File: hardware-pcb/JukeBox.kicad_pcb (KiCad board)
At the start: 2 copper layers, 100 x 100 mm, 97 parts, among them J1 USB4105-GF-A, Q1 Q_NPN_ECB, SW1 SW_SPST, SW10 SW_SPST, SW11 SW_SPST, SW12 SW_SPST, SW2 SW_SPST, SW3 SW_SPST, SW4 SW_SPST, SW5 SW_SPST, SW6 SW_SPST, SW7 SW_SPST, SW8 SW_SPST, SW9 SW_SPST, U1 NCP1117-3.3_SOT223, U2 W25Q128JVS, U3 RP2040, U4 st7789v, Y1 ECS-120-20-33-AEL-TR

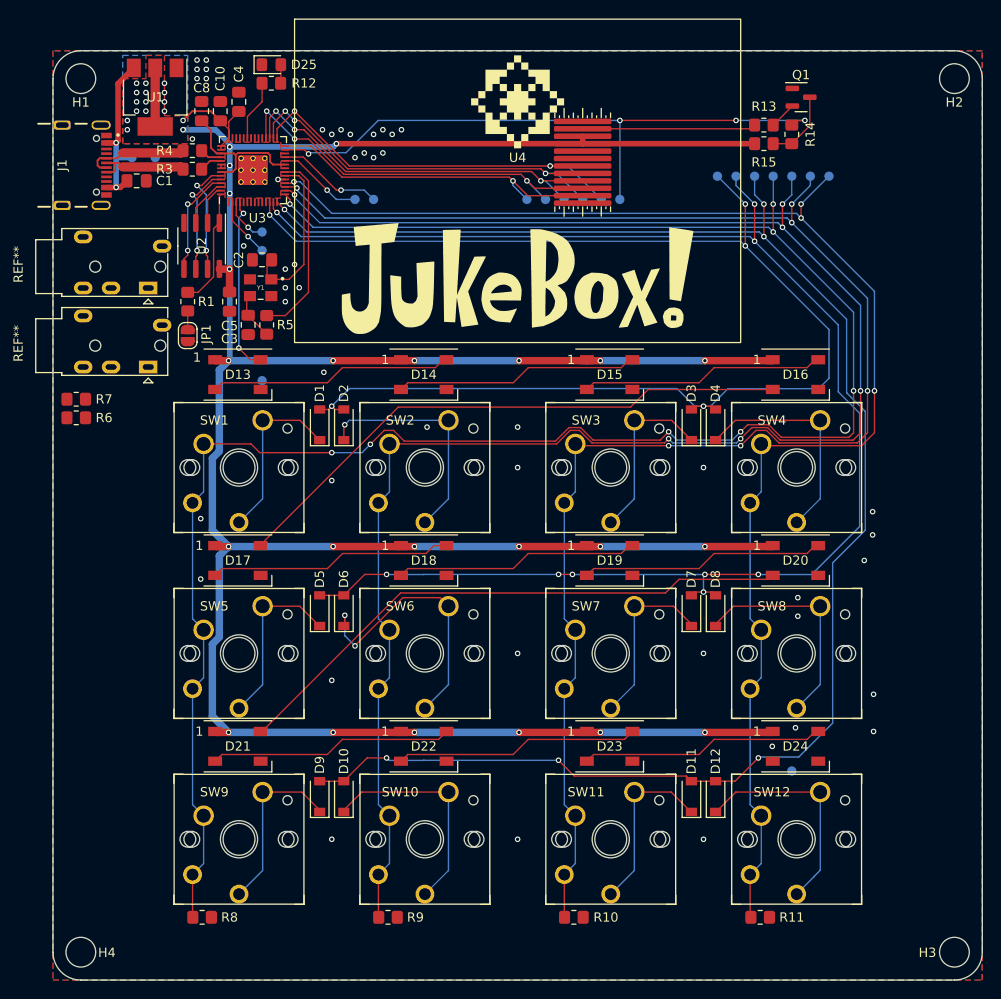
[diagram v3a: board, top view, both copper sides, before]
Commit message: change mounting to via pads
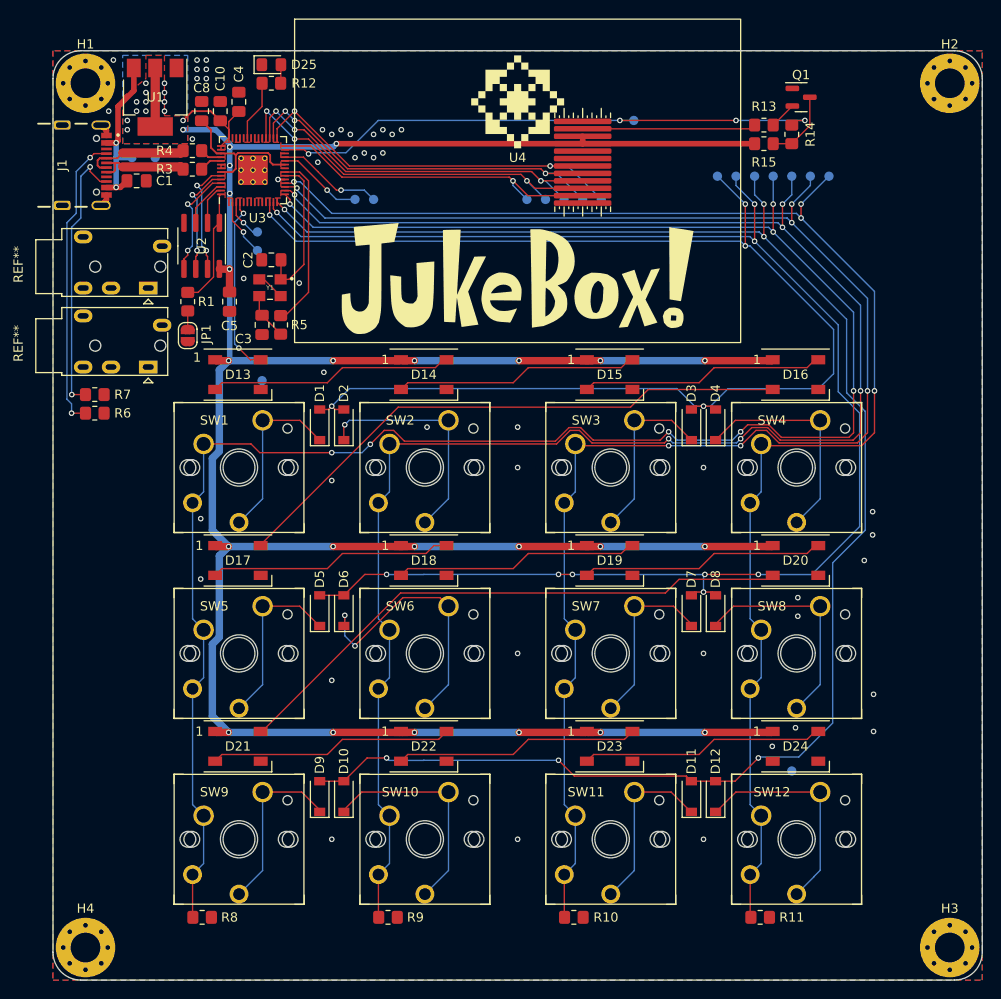
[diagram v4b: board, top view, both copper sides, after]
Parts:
- H1, H2, H3, H4: footprint MountingHole:MountingHole_3.2mm_M3 -> MountingHole:MountingHole_3.2mm_M3_Pad_Via
- moved TP31 8.63 mm to (125.1, 74.5)
- moved R6 2.06 mm to (67.1, 106.0)
- moved R7 2.06 mm to (67.1, 104.0)
- moved C3 1.50 mm to (85.1, 96.5)
- moved R5 1.50 mm to (87.1, 96.5)
- moved C2 1.00 mm to (86.1, 89.5)
- moved Y1 1.00 mm to (85.9, 92.5)
- moved H1 0.71 mm to (66.1, 70.5)
- moved H2 0.71 mm to (159.1, 70.5)
- moved H3 0.71 mm to (159.1, 163.5)
- moved H4 0.71 mm to (66.1, 163.5)
- moved TP11 0.50 mm to (84.6, 86.5)
- moved TP12 0.50 mm to (84.6, 88.5)
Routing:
- net Net-(J1-CC1): track 0.00 -> 32.2 mm, vias 0 -> 2
- net Net-(J1-CC2): track 0.00 -> 29.5 mm, vias 0 -> 2
- net /GPIO16: track 67.8 -> 60.8 mm
- net GND: track 8.39 -> 14.2 mm, vias 49 -> 48
- net /XOUT: track 20.5 -> 19.0 mm
- net /XIN: track 17.9 -> 16.5 mm
- net /GPIO9: track 142.8 -> 143.5 mm
- net /DBGTX: track 4.95 -> 4.45 mm
- net +3V3: vias 39 -> 37

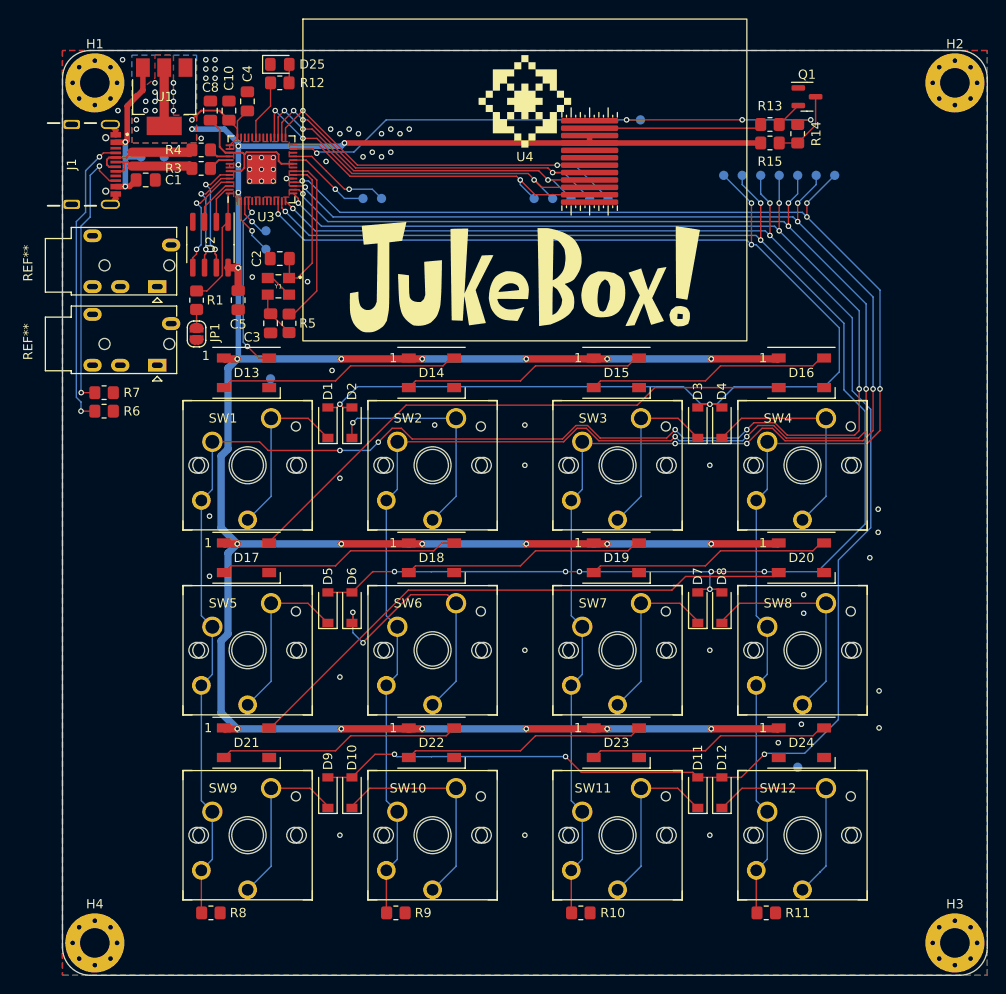
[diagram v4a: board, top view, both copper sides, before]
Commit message: rearrange parts, fix nets
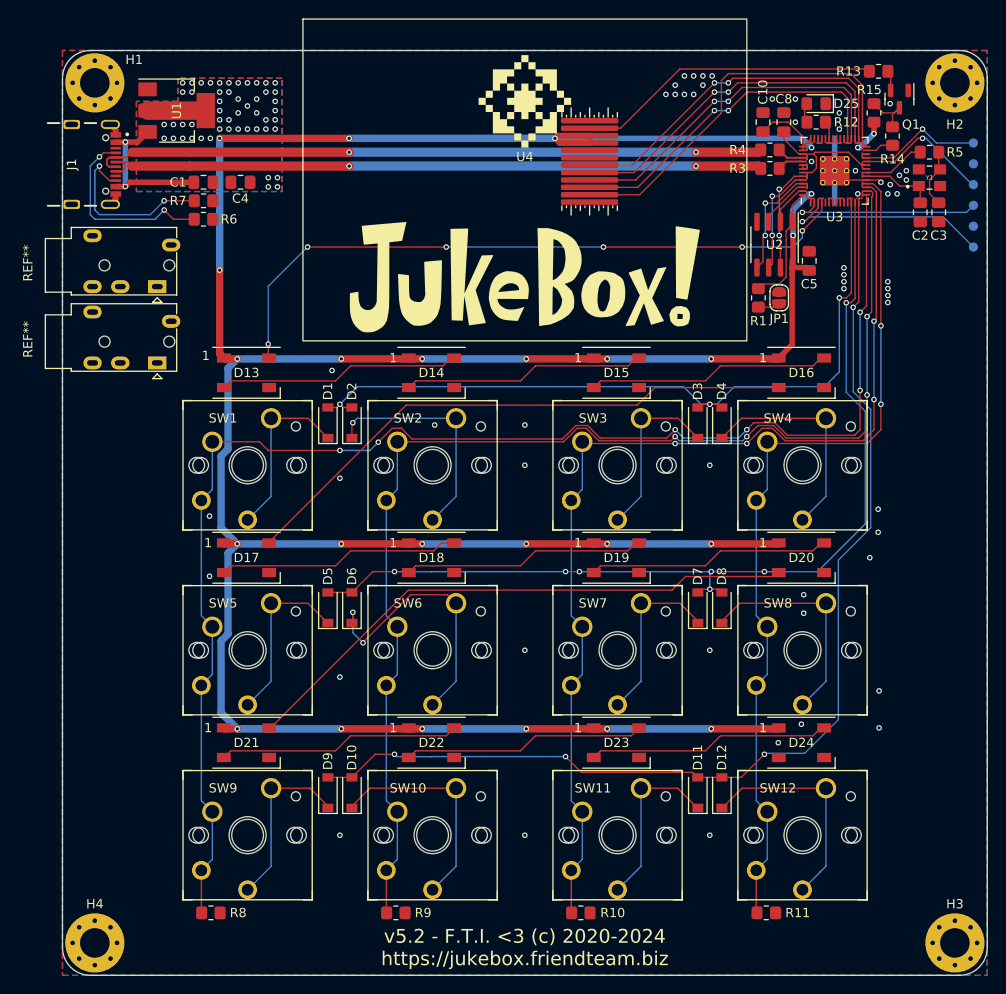
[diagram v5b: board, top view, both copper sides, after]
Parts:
- removed TP1, TP2, TP24, TP25, TP26, TP27, TP31, TP32, TP33, TP34, TP35, TP36, TP41, TP42: TestPoint, TestPoint:TestPoint_Pad_D1.0mm
- removed the TP21 at (138.1, 80.5)
- removed the TP23 at (134.1, 80.5)
- added TP12: TestPoint, TestPoint:TestPoint_Pad_D1.0mm, B.Cu at (161.1, 79.2)
- H1, H2, H3, H4: value MountingHole -> MountingHole_Pad
- moved TP13 76.6 mm to (161.1, 83.8)
- moved TP11 76.5 mm to (161.1, 88.2)
- moved C3 73.2 mm to (157.3, 84.5)
- moved R5 71.7 mm to (156.3, 78.0), turned to 0 degrees
- moved Y1 71.4 mm to (156.3, 80.8), turned to 0 degrees
- moved C2 69.4 mm to (155.3, 84.5), turned to -90 degrees
- moved TP23 66.0 mm to (161.1, 81.5)
- moved TP21 64.3 mm to (161.1, 77.0)
- moved JP1 63.1 mm to (140.1, 93.8), turned to -90 degrees
- moved C8 62.0 mm to (140.6, 74.8)
- moved U3 62.0 mm to (146.1, 80.0)
- moved C5 61.9 mm to (143.3, 89.8), turned to 90 degrees
- moved R3 61.5 mm to (139.1, 79.8)
- moved R4 61.5 mm to (139.1, 77.8)
- moved U2 61.0 mm to (139.6, 88.0)
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- renumbered TP12 to TP13, TP13 to TP21, TP14 to TP23
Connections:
- H1 pad 1: (no net) -> GND
- H2 pad 1: (no net) -> GND
- H3 pad 1: (no net) -> GND
- H4 pad 1: (no net) -> GND
- TP22 pad 1: /GPIO10 -> GND
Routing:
- net /GPIO15: track 155.6 -> 94.1 mm, vias 4 -> 2
- net /USB_D-: track 11.2 -> 72.7 mm, vias 0 -> 2
- net /USB_D+: track 11.2 -> 72.7 mm, vias 0 -> 2
- net /GPIO9: track 143.5 -> 82.1 mm, vias 5 -> 3
- net /GPIO10: track 163.2 -> 102.3 mm, vias 9 -> 7
- net /GPIO14: track 174.7 -> 113.9 mm, vias 6 -> 4
- net /GPIO11: track 179.0 -> 118.3 mm, vias 6 -> 4
- net /GPIO13: track 194.1 -> 134.0 mm, vias 6 -> 4
- net /GPIO12: track 214.3 -> 154.4 mm, vias 8 -> 6
- net /GPIO16: track 60.8 -> 3.04 mm, vias 4 -> 0
- net /GPIO2: track 19.3 -> 72.4 mm, vias 2 -> 6
- net +3V3: track 336.0 -> 364.4 mm, vias 37 -> 81
- net GND: track 14.2 -> 33.6 mm, vias 48 -> 54
- net /DBGTX: track 4.45 -> 23.0 mm
- net /DBGRX: track 6.32 -> 20.8 mm
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
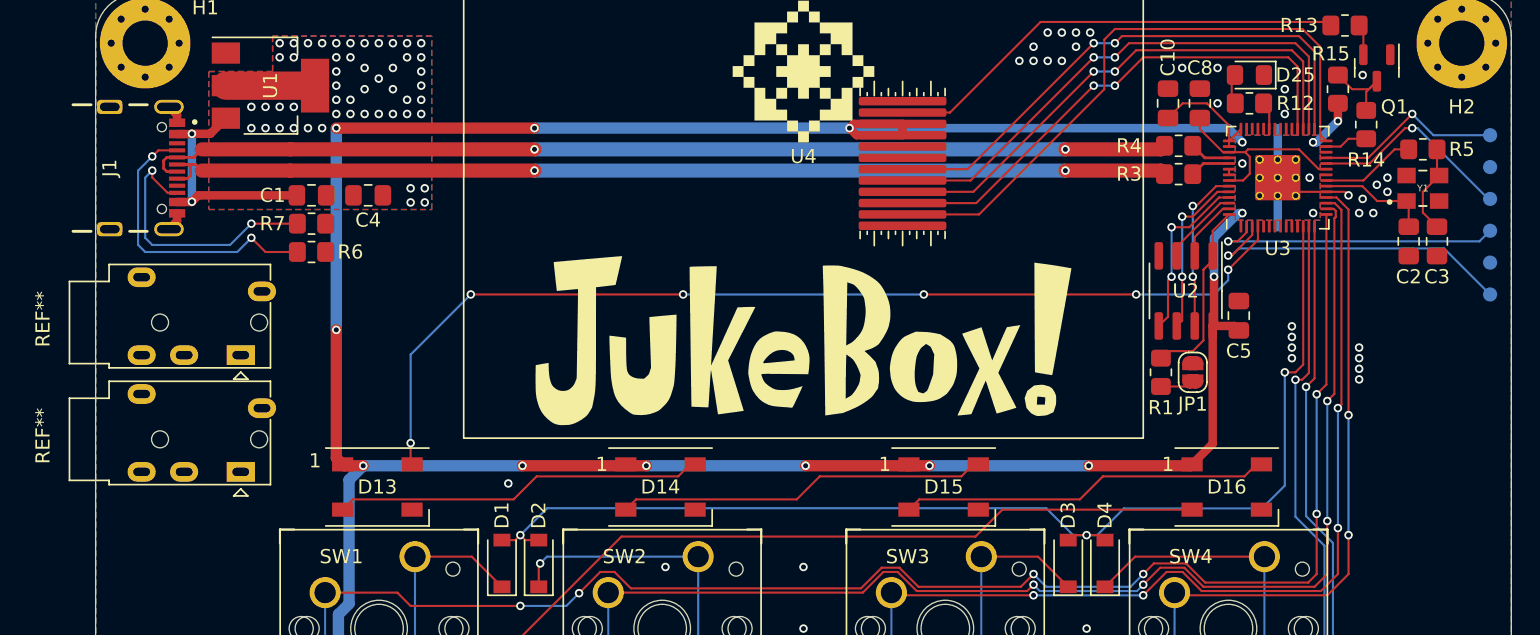
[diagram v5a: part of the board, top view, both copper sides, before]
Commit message: add headphone jacks for i2c busses for expansion
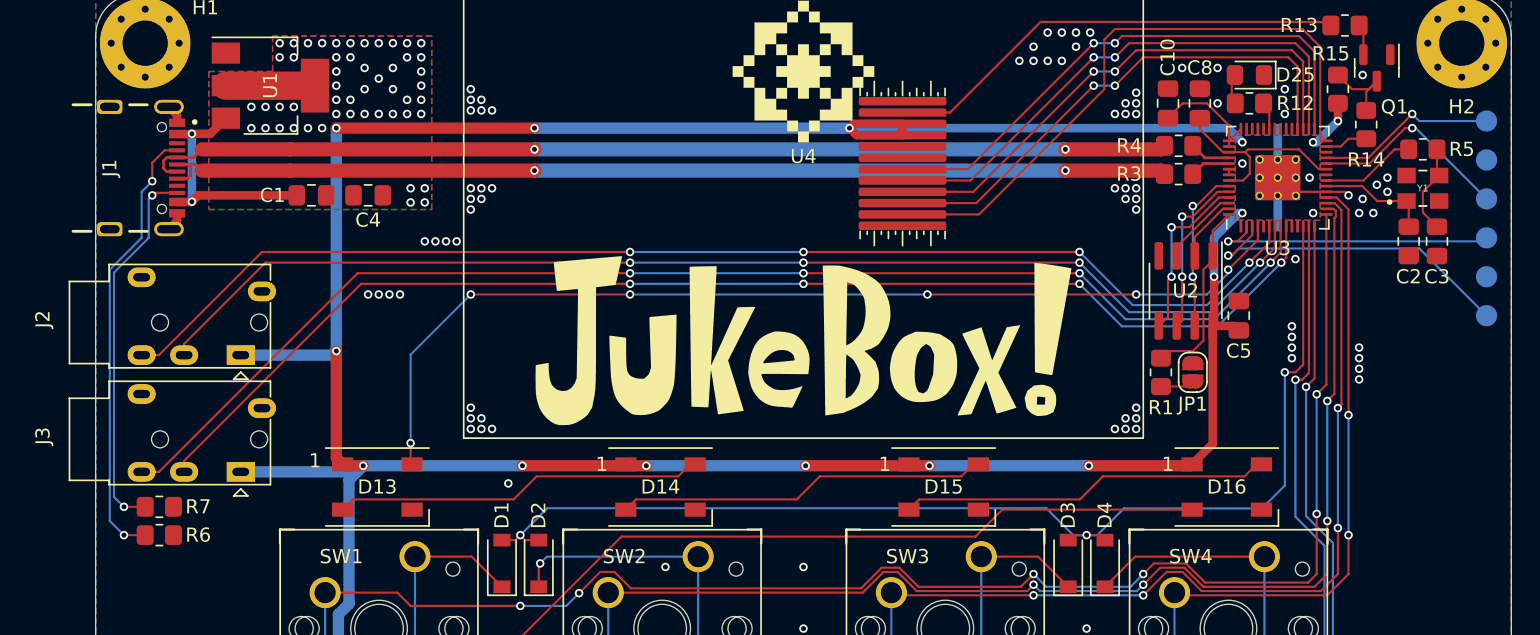
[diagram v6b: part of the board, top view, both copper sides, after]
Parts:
- removed REF** (x2): Jack_3.5mm_PJ320E_Horizontal, Connector_Audio:Jack_3.5mm_PJ320E_Horizontal
- added J2: AudioJack4_Ground, Connector_Audio:Jack_3.5mm_PJ320E_Horizontal, F.Cu at (72.8, 92.5)
- added J3: AudioJack4_Ground, Connector_Audio:Jack_3.5mm_PJ320E_Horizontal, F.Cu at (72.8, 100.8)
- TP11, TP12, TP13, TP21, TP22, TP23: footprint TestPoint:TestPoint_Pad_D1.0mm -> TestPoint:TestPoint_Pad_D1.5mm
- moved R6 22.7 mm to (67.1, 105.2)
- moved R7 22.7 mm to (67.1, 103.2)
- moved TP11 1.52 mm to (160.8, 89.8)
- moved TP21 1.03 mm to (160.8, 76.0)
- moved TP22 1.03 mm to (160.8, 87.0)
- moved TP12 0.56 mm to (160.8, 78.8)
- moved TP13 0.56 mm to (160.8, 84.2)
- moved TP23 0.25 mm to (160.8, 81.5)
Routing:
- net /GPIO6: track 0.00 -> 91.4 mm, vias 0 -> 4
- net /GPIO7: track 0.00 -> 89.3 mm, vias 0 -> 4
- net /GPIO4: track 0.00 -> 87.2 mm, vias 0 -> 4
- net /GPIO5: track 0.00 -> 85.1 mm, vias 0 -> 4
- net +3V3: track 364.4 -> 380.1 mm
- net Net-(J1-CC1): track 20.9 -> 31.6 mm
- net Net-(J1-CC2): track 19.2 -> 26.7 mm
- net /DBGSD: track 13.5 -> 12.8 mm
- net GND: vias 54 -> 99

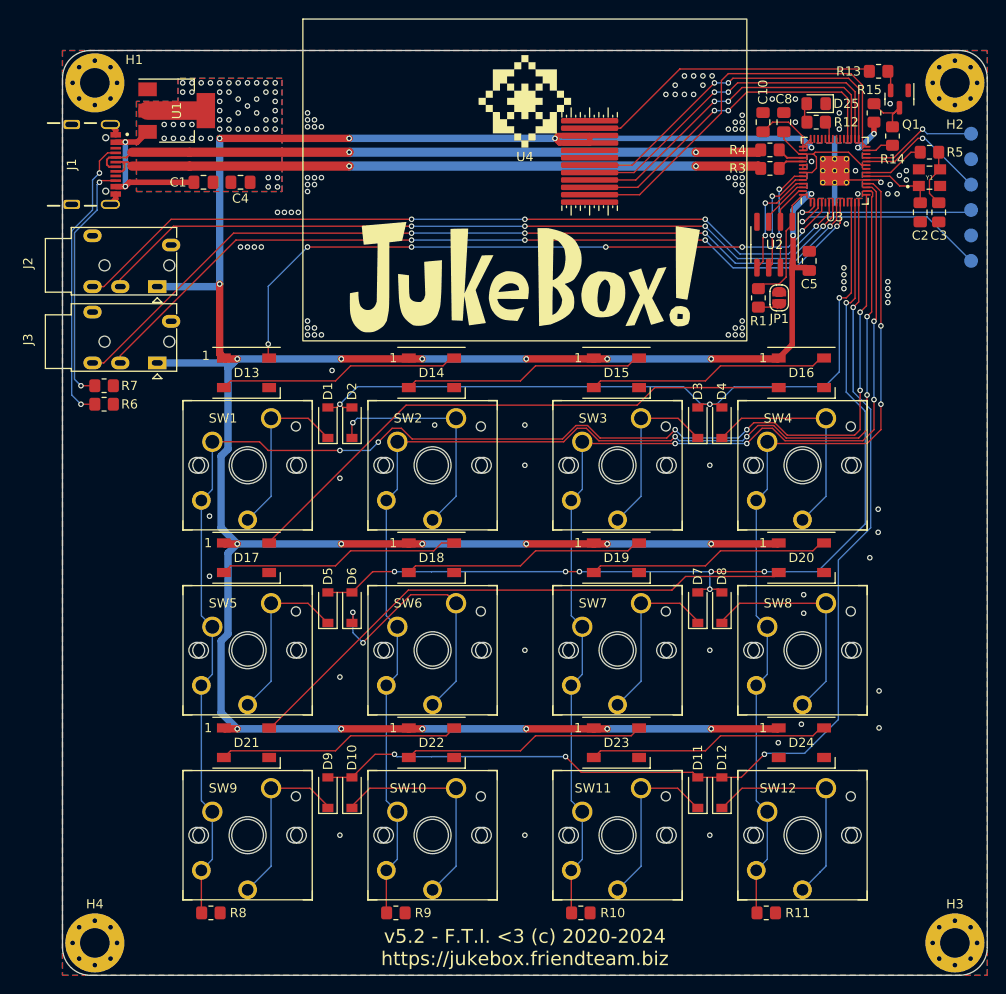
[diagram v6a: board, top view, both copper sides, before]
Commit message: fix screen footprint, prepare for fab
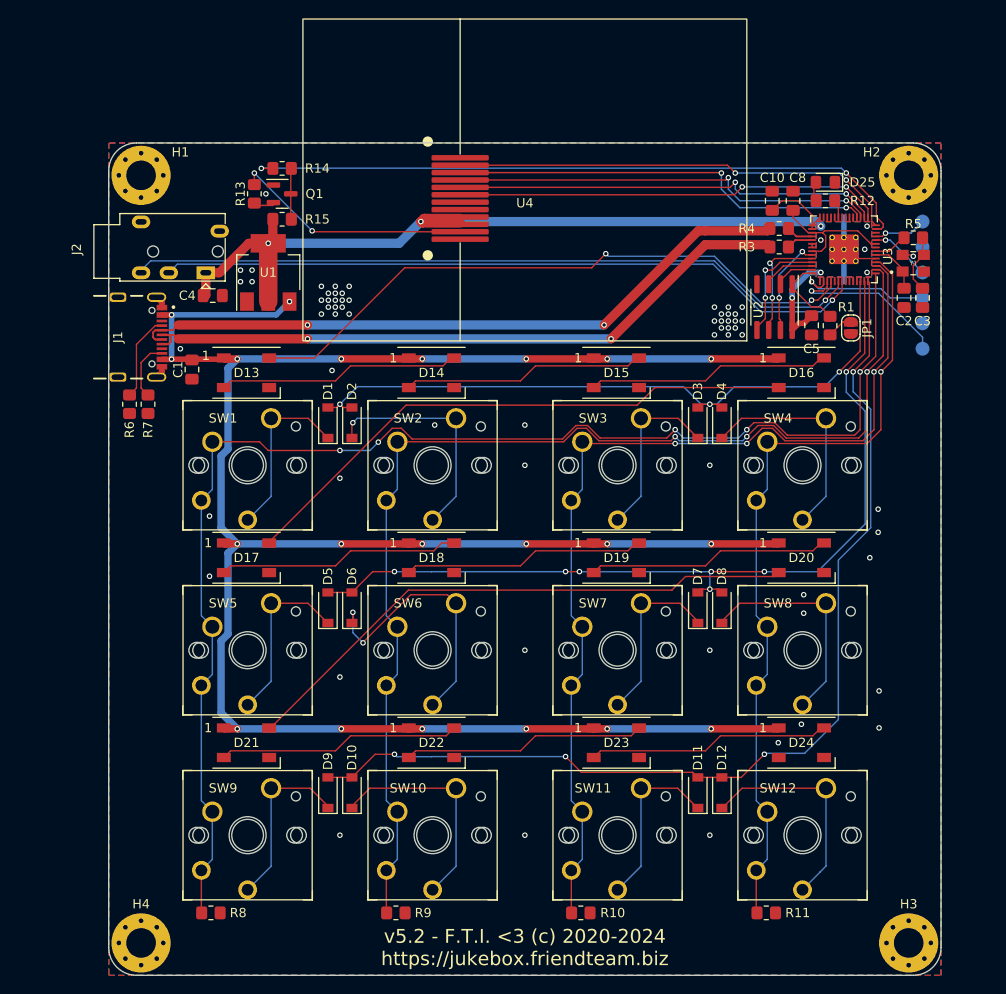
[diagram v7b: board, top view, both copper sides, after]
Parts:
- removed the G*** at (112.6, 72.5)
- removed the G1 at (112.6, 91.5)
- removed J3: AudioJack4_Ground, Connector_Audio:Jack_3.5mm_PJ320E_Horizontal
- moved R13 68.8 mm to (83.3, 82.5), turned to 90 degrees
- moved Q1 67.5 mm to (86.3, 82.5), turned to 0 degrees
- moved R14 66.1 mm to (86.3, 79.8), turned to 0 degrees
- moved R15 65.0 mm to (86.3, 85.2), turned to 0 degrees
- moved G*** 22.2 mm to (112.6, 94.8)
- moved C1 20.3 mm to (76.6, 101.5), turned to -90 degrees
- moved U1 20.1 mm to (84.8, 91.0), turned to 90 degrees
- moved J1 19.3 mm to (68.6, 98.0)
- moved C4 12.6 mm to (78.8, 93.5), turned to 0 degrees
- moved H1 11.2 mm to (71.1, 80.5)
- moved H2 11.2 mm to (154.1, 80.5)
- moved TP11 10.9 mm to (155.6, 99.2)
- moved TP12 10.9 mm to (155.6, 88.2)
- moved TP13 10.9 mm to (155.6, 93.8)
- moved TP21 10.9 mm to (155.6, 85.5)
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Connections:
- D13 pad 1: +3V3 -> VBUS
- D14 pad 1: +3V3 -> VBUS
- D15 pad 1: +3V3 -> VBUS
- D16 pad 1: +3V3 -> VBUS
- D17 pad 1: +3V3 -> VBUS
- D18 pad 1: +3V3 -> VBUS
- D19 pad 1: +3V3 -> VBUS
- D20 pad 1: +3V3 -> VBUS
- D21 pad 1: +3V3 -> VBUS
- D22 pad 1: +3V3 -> VBUS
- D23 pad 1: +3V3 -> VBUS
- D24 pad 1: +3V3 -> VBUS
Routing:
- net +3V3: track 380.1 -> 113.1 mm, vias 81 -> 9
- net VBUS: track 17.4 -> 250.7 mm, vias 2 -> 21
- net /GPIO6: track 91.4 -> 0.00 mm, vias 4 -> 0
- net /GPIO7: track 89.3 -> 0.00 mm, vias 4 -> 0
- net /GPIO16: track 3.04 -> 73.1 mm, vias 0 -> 2
- net Net-(J1-CC1): track 31.6 -> 9.38 mm, vias 2 -> 0
- net Net-(J1-CC2): track 26.7 -> 6.48 mm, vias 2 -> 0
- net /GPIO21: track 36.9 -> 46.2 mm
- net /GPIO20: track 37.5 -> 46.2 mm
- net /GPIO9: track 82.1 -> 73.6 mm
- net /GPIO10: track 102.3 -> 94.0 mm
- net /GPIO12: track 154.4 -> 146.3 mm, vias 6 -> 5
- net /GPIO19: track 38.2 -> 46.3 mm
- net /GPIO15: track 94.1 -> 86.1 mm, vias 2 -> 1
- net /GPIO13: track 134.0 -> 126.0 mm, vias 4 -> 3
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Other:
- board size 100 x 100 mm -> 90 x 90 mm

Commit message: minor updates for production
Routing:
- net VBUS: track 250.7 -> 253.6 mm
